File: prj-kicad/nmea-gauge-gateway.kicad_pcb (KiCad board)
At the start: 2 copper layers, 80 x 50 mm, 1 part, among them P2 CONN_8

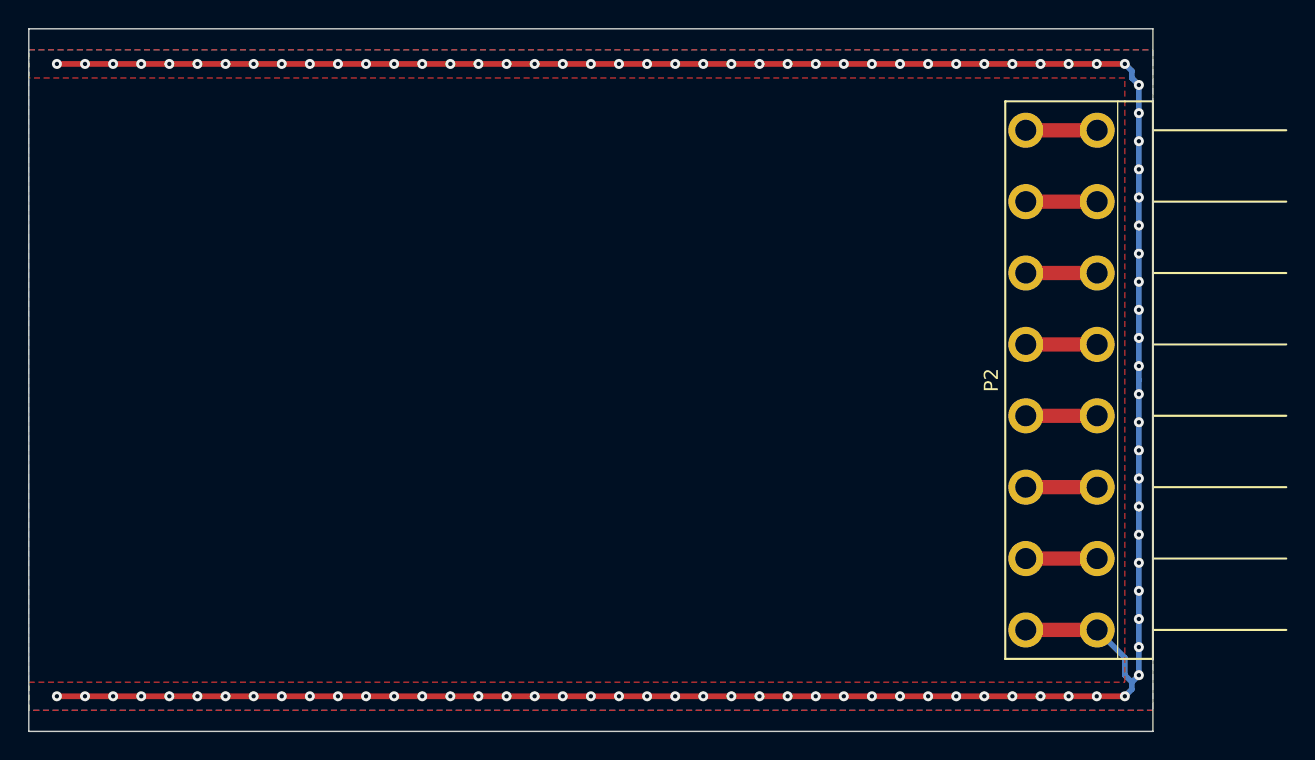
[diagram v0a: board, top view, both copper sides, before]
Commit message: = ADD: Insert analog inputs/outputs for gauge sensors
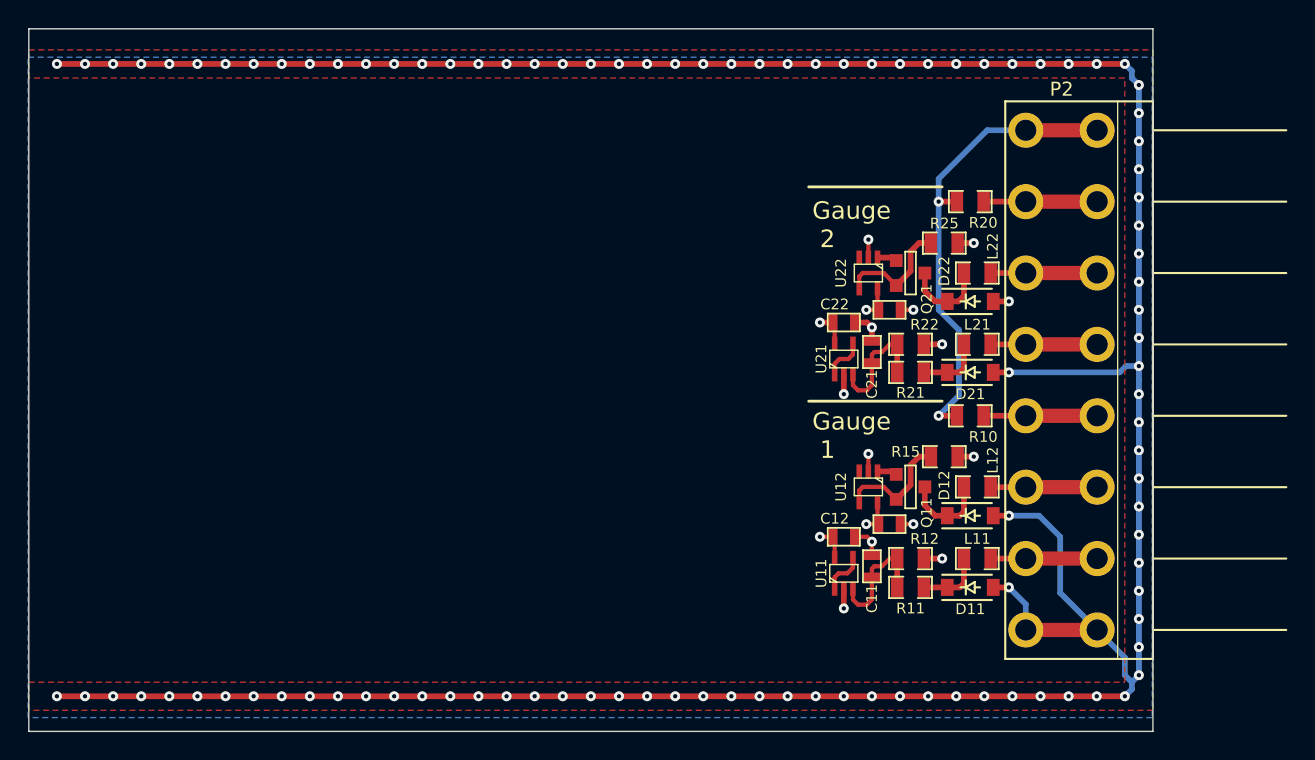
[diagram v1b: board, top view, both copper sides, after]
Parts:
- added C11: 100nF, nmea-gauge-gateway:SMD0603, F.Cu at (168.5, 118.2)
- added C12: 100nF, nmea-gauge-gateway:SMD0603, F.Cu at (166.5, 116.2)
- added C13: 100nF, nmea-gauge-gateway:SMD0603, F.Cu at (169.8, 115.2)
- added C21: 100nF, nmea-gauge-gateway:SMD0603, F.Cu at (168.5, 103.0)
- added C22: 100nF, nmea-gauge-gateway:SMD0603, F.Cu at (166.5, 100.9)
- added C23: 100nF, nmea-gauge-gateway:SMD0603, F.Cu at (169.8, 100.0)
- added D11: TVS, nmea-gauge-gateway:SOD-123, F.Cu at (175.5, 119.8)
- added D12: TVS, nmea-gauge-gateway:SOD-123, F.Cu at (175.5, 114.7)
- added D21: TVS, nmea-gauge-gateway:SOD-123, F.Cu at (175.5, 104.5)
- added D22: TVS, nmea-gauge-gateway:SOD-123, F.Cu at (175.5, 99.4)
- added L11: 680nH, nmea-gauge-gateway:SMD0805, F.Cu at (176.0, 117.7)
- added L12: 680nH, nmea-gauge-gateway:SMD0805, F.Cu at (176.0, 112.6)
- added L21: 680nH, nmea-gauge-gateway:SMD0805, F.Cu at (176.0, 102.5)
- added L22: 680nH, nmea-gauge-gateway:SMD0805, F.Cu at (176.0, 97.4)
- added Q11: T_NPN, nmea-gauge-gateway:SOT23-3, F.Cu at (171.2, 112.6)
- added Q21: T_NPN, nmea-gauge-gateway:SOT23-3, F.Cu at (171.2, 97.4)
- added R10: 10k, nmea-gauge-gateway:SMD0805, F.Cu at (175.5, 107.5)
- added R11: 1M, nmea-gauge-gateway:SMD0805, F.Cu at (171.2, 119.8)
- added R12: 100k, nmea-gauge-gateway:SMD0805, F.Cu at (171.2, 117.7)
- added R15: 1, nmea-gauge-gateway:SMD0805, F.Cu at (173.7, 110.5)
- added R20: 10k, nmea-gauge-gateway:SMD0805, F.Cu at (175.5, 92.3)
- added R21: 1M, nmea-gauge-gateway:SMD0805, F.Cu at (171.2, 104.5)
- added R22: 100k, nmea-gauge-gateway:SMD0805, F.Cu at (171.2, 102.5)
- added R25: 1, nmea-gauge-gateway:SMD0805, F.Cu at (173.7, 95.2)
- added U11: MCP6001, nmea-gauge-gateway:SC70-5, F.Cu at (166.5, 118.8)
- added U12: MCP6001, nmea-gauge-gateway:SC70-5, F.Cu at (168.2, 112.6)
- added U21: MCP6001, nmea-gauge-gateway:SC70-5, F.Cu at (166.5, 103.5)
- added U22: MCP6001, nmea-gauge-gateway:SC70-5, F.Cu at (168.2, 97.4)
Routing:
- net GND: track 207.7 -> 331.7 mm, vias 100 -> 116
- net +3.3V: track 0.00 -> 32.5 mm, vias 0 -> 4
- net +VIn: track 5.08 -> 33.4 mm, vias 0 -> 2
- net Net-(C11-Pad1): track 0.00 -> 9.09 mm
- net Net-(C21-Pad1): track 0.00 -> 8.70 mm
- net Net-(Q11-Pad2): track 0.00 -> 8.51 mm
- net Net-(Q21-Pad2): track 0.00 -> 8.49 mm
- net Net-(D12-Pad1): track 0.00 -> 6.28 mm
- net Net-(D22-Pad1): track 0.00 -> 6.16 mm
- net Net-(D11-Pad1): track 0.00 -> 4.72 mm
- net Net-(D21-Pad1): track 0.00 -> 4.67 mm
- net GAUGE2: track 0.00 -> 3.11 mm
- net GAUGE1: track 0.00 -> 3.10 mm
- net GAUGE2_REF: track 5.08 -> 8.08 mm
- net GAUGE1_REF: track 5.08 -> 8.08 mm
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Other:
- copper layers 2 -> 4
- board text added: "Gauge 1"
- board text added: "Gauge 2"

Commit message: = ADD: Insert power supply
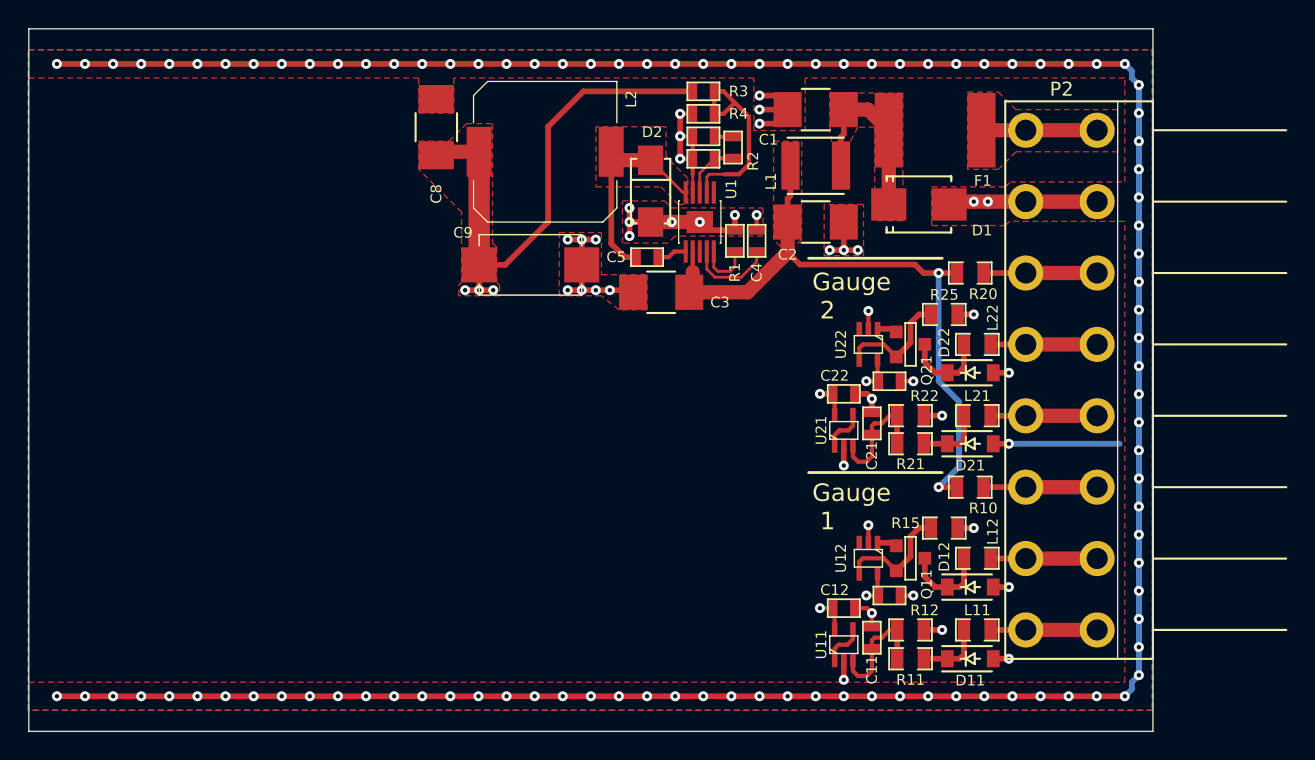
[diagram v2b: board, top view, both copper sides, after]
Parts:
- added C1: 2,2uF, nmea-gauge-gateway:C_1210, F.Cu at (164.5, 85.8)
- added C2: 2,2uF, nmea-gauge-gateway:C_1210, F.Cu at (164.5, 93.8)
- added C3: 2,2uF, nmea-gauge-gateway:C_1210, F.Cu at (153.5, 98.8)
- added C4: 10nF, nmea-gauge-gateway:SMD0603, F.Cu at (160.3, 95.1)
- added C5: 100nF, nmea-gauge-gateway:C_0603, F.Cu at (152.5, 96.2)
- added C6: n/a, nmea-gauge-gateway:SMD0603, F.Cu at (156.5, 89.2)
- added C7: 4700pF, nmea-gauge-gateway:SMD0603, F.Cu at (156.5, 87.7)
- added C8: C, nmea-gauge-gateway:C_1210, F.Cu at (137.5, 87.0)
- added C9: 220uF, nmea-gauge-gateway:C_TPB_D4, F.Cu at (144.2, 96.8)
- added D1: TVS, nmea-gauge-gateway:D_SMB, F.Cu at (171.8, 92.5)
- added D2: MBRA340, nmea-gauge-gateway:DO214AC, F.Cu at (152.8, 91.5)
- added F1: 2920L050DR, nmea-gauge-gateway:SMD_2920, F.Cu at (173.0, 87.2)
- added L1: INDUCTOR, nmea-gauge-gateway:I_TYS4012, F.Cu at (164.5, 89.8)
- added L2: 27uH, nmea-gauge-gateway:I_MSS1048, F.Cu at (145.2, 88.8)
- added R1: 100k, nmea-gauge-gateway:R_0603, F.Cu at (158.8, 95.1)
- added R2: 20k, nmea-gauge-gateway:R_0603, F.Cu at (158.6, 88.5)
- added R3: 47k, nmea-gauge-gateway:R_0603, F.Cu at (156.5, 84.5)
- added R4: 15k, nmea-gauge-gateway:R_0603, F.Cu at (156.5, 86.0)
- added U1: TPS54160A, nmea-gauge-gateway:MSOP10p, F.Cu at (156.2, 93.8)
- moved L12 5.08 mm to (176.0, 117.7)
- moved Q11 5.08 mm to (171.2, 117.7)
- moved U12 5.08 mm to (168.2, 117.7)
- moved C11 5.08 mm to (168.5, 123.3)
- moved C12 5.08 mm to (166.5, 121.2)
- moved C13 5.08 mm to (169.8, 120.3)
- moved C21 5.08 mm to (168.5, 108.1)
- moved C22 5.08 mm to (166.5, 106.0)
- moved C23 5.08 mm to (169.8, 105.1)
- moved D11 5.08 mm to (175.5, 124.8)
- moved D12 5.08 mm to (175.5, 119.7)
- moved D21 5.08 mm to (175.5, 109.5)
- moved D22 5.08 mm to (175.5, 104.5)
- moved L11 5.08 mm to (176.0, 122.8)
- moved L21 5.08 mm to (176.0, 107.5)
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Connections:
- P2 pad 1: GND -> GAUGE1_IN
- P2 pad 2: GAUGE1_IN -> GAUGE1_OUT
- P2 pad 3: GAUGE1_OUT -> GAUGE1_REF
- P2 pad 4: GAUGE1_REF -> GAUGE2_IN
- P2 pad 5: GAUGE2_IN -> GAUGE2_OUT
- P2 pad 6: GAUGE2_OUT -> GAUGE2_REF
- P2 pad 7: GAUGE2_REF -> GND
- R10 pad 1: +VIn -> +VInP
- R20 pad 1: +VIn -> +VInP
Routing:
- net +3.3V: track 32.5 -> 101.4 mm, vias 4 -> 7
- net +VInP: track 0.00 -> 47.8 mm, vias 0 -> 2
- net GND: track 331.7 -> 379.0 mm, vias 116 -> 141
- net +VIn: track 33.4 -> 8.23 mm, vias 2 -> 0
- net /Power Supply/3V3_SW: track 0.00 -> 15.2 mm
- net Net-(R3-Pad2): track 0.00 -> 14.5 mm
- net /Power Supply/FUSED_VIN: track 0.00 -> 13.2 mm
- net Net-(C4-Pad1): track 0.00 -> 6.22 mm
- net Net-(C6-Pad1): track 0.00 -> 4.19 mm
- net Net-(R1-Pad1): track 0.00 -> 3.96 mm
- net Net-(C5-Pad1): track 0.00 -> 2.15 mm
- net Net-(C7-Pad1): track 0.00 -> 1.36 mm
- added copper zone on F.Cu, net +3.3V
- added copper zone on F.Cu, net +VIn
- added copper zone on F.Cu, net +VInP
- added copper zone on F.Cu, net /Power Supply/3V3_SW
- added copper zone on F.Cu, net /Power Supply/FUSED_VIN
